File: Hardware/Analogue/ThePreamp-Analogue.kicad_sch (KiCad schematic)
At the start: 19 parts, among them J1 B1 Relays, J10 I2C (FUTURE USE), J14 12V, J15 8V, J2 PWR AMP L 12V TRIGGER, J3 PWR AMP L SWITCH, J4 PWR AMP R 12V TRIGGER, J5 PWR AMP R SWITCH, J6 PWR AMP TEMP NTC L, J7 PWR AMP TEMP NTC R, J8 MUSES 72320 (SPI), U1 AGQ20T03, U2 AGQ20T03, U3 ULN2803ADWR, U4 MCP23008-E_SO

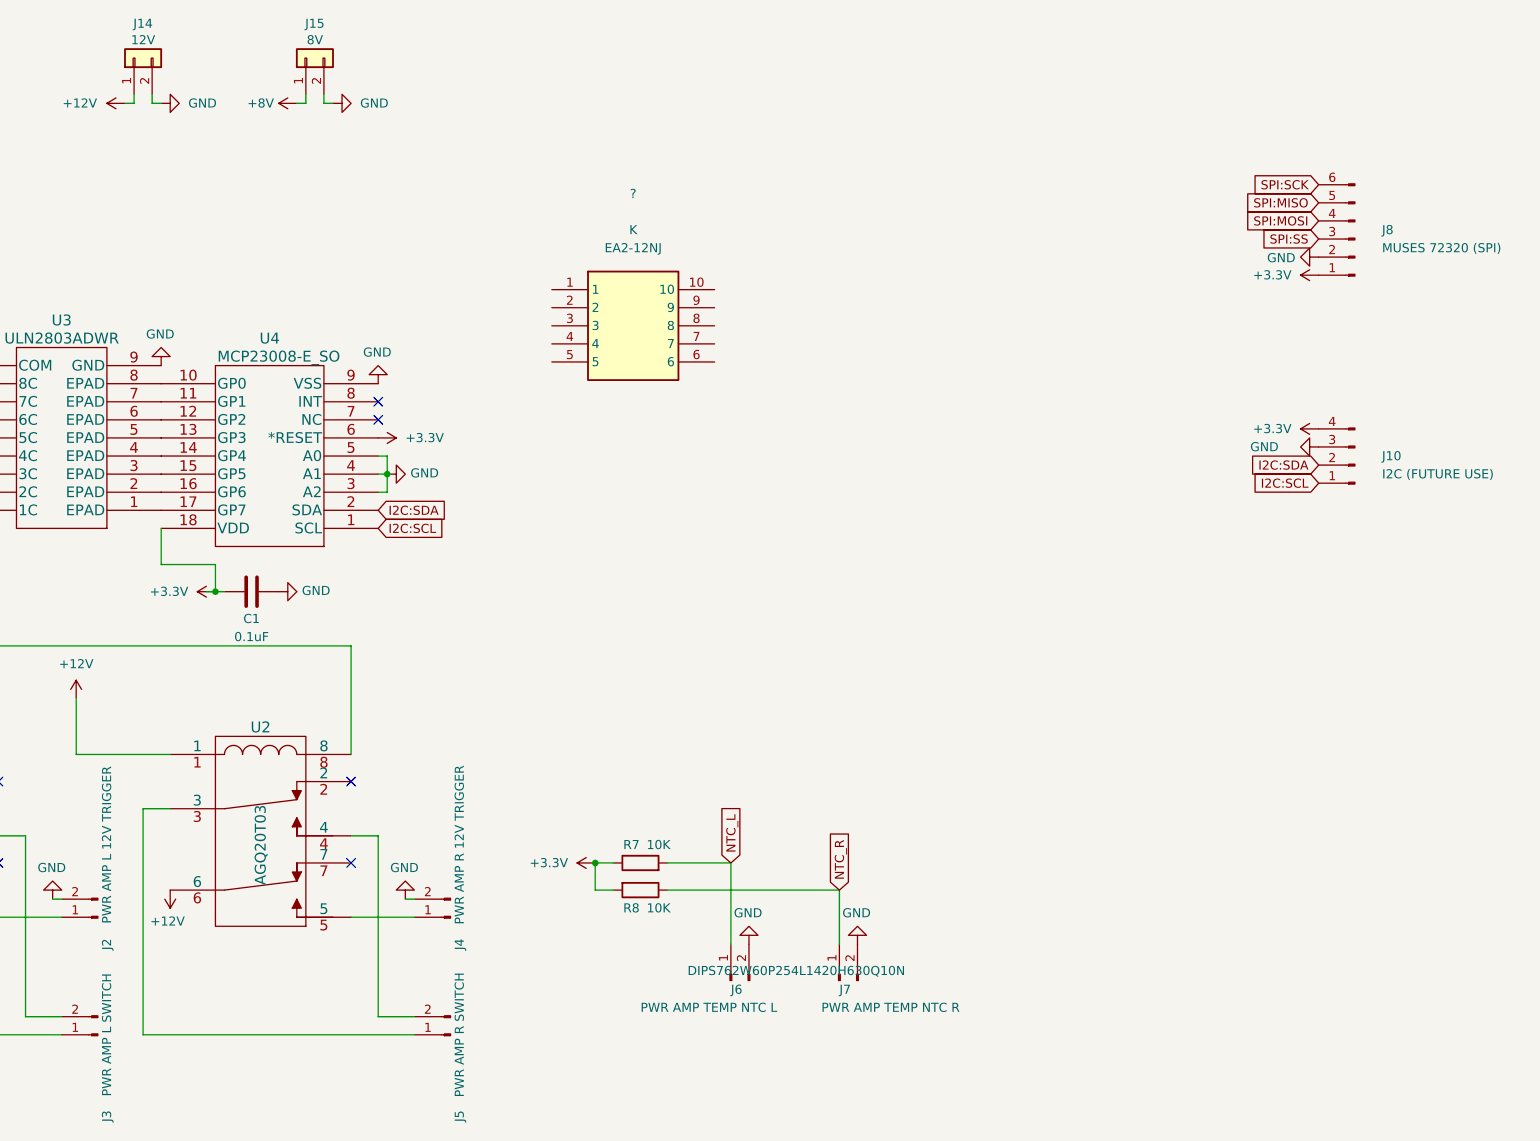
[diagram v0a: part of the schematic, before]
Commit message: added footprint to rca connector
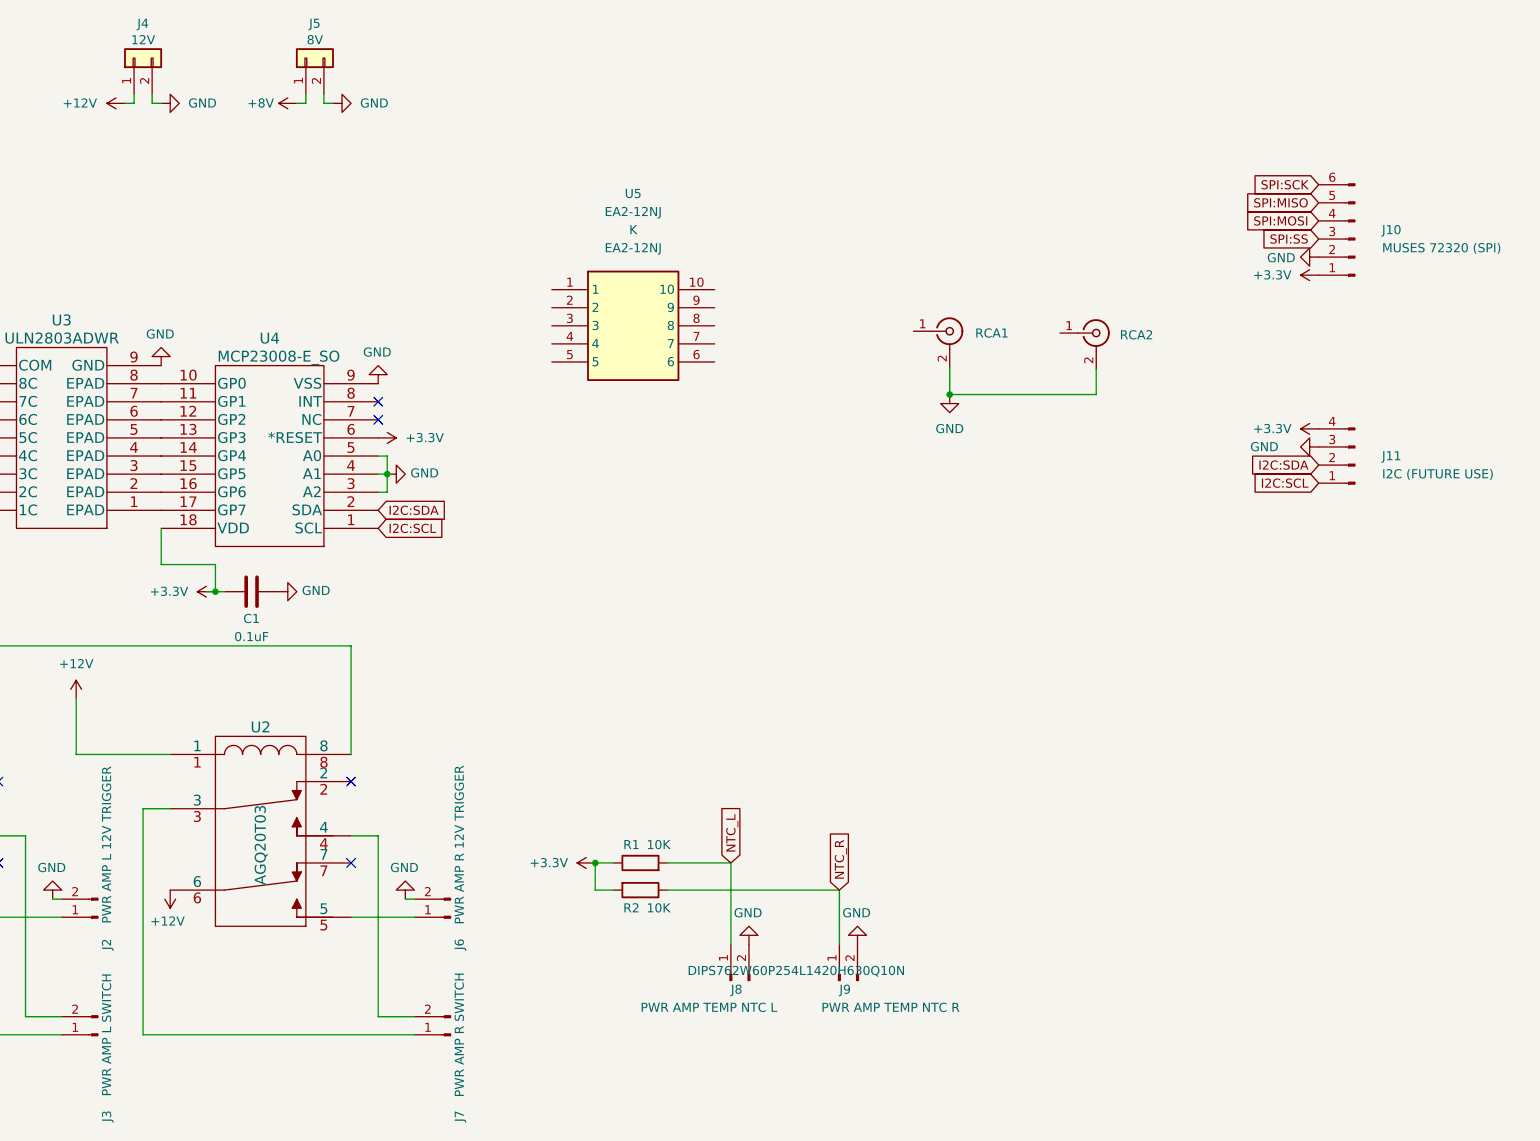
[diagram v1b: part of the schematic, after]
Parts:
- added RCA1, RCA2: (no value), symbol Connector:RCA_Connector_ALI
- U5: renamed from ?; value (none) -> EA2-12NJ
- renumbered J8 to J10, J10 to J11, J14 to J4, J15 to J5, J4 to J6, J5 to J7, J6 to J8, J7 to J9, R7 to R1, R8 to R2
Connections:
- net GND: now also RCA1.2 (Ext), RCA2.2 (Ext)

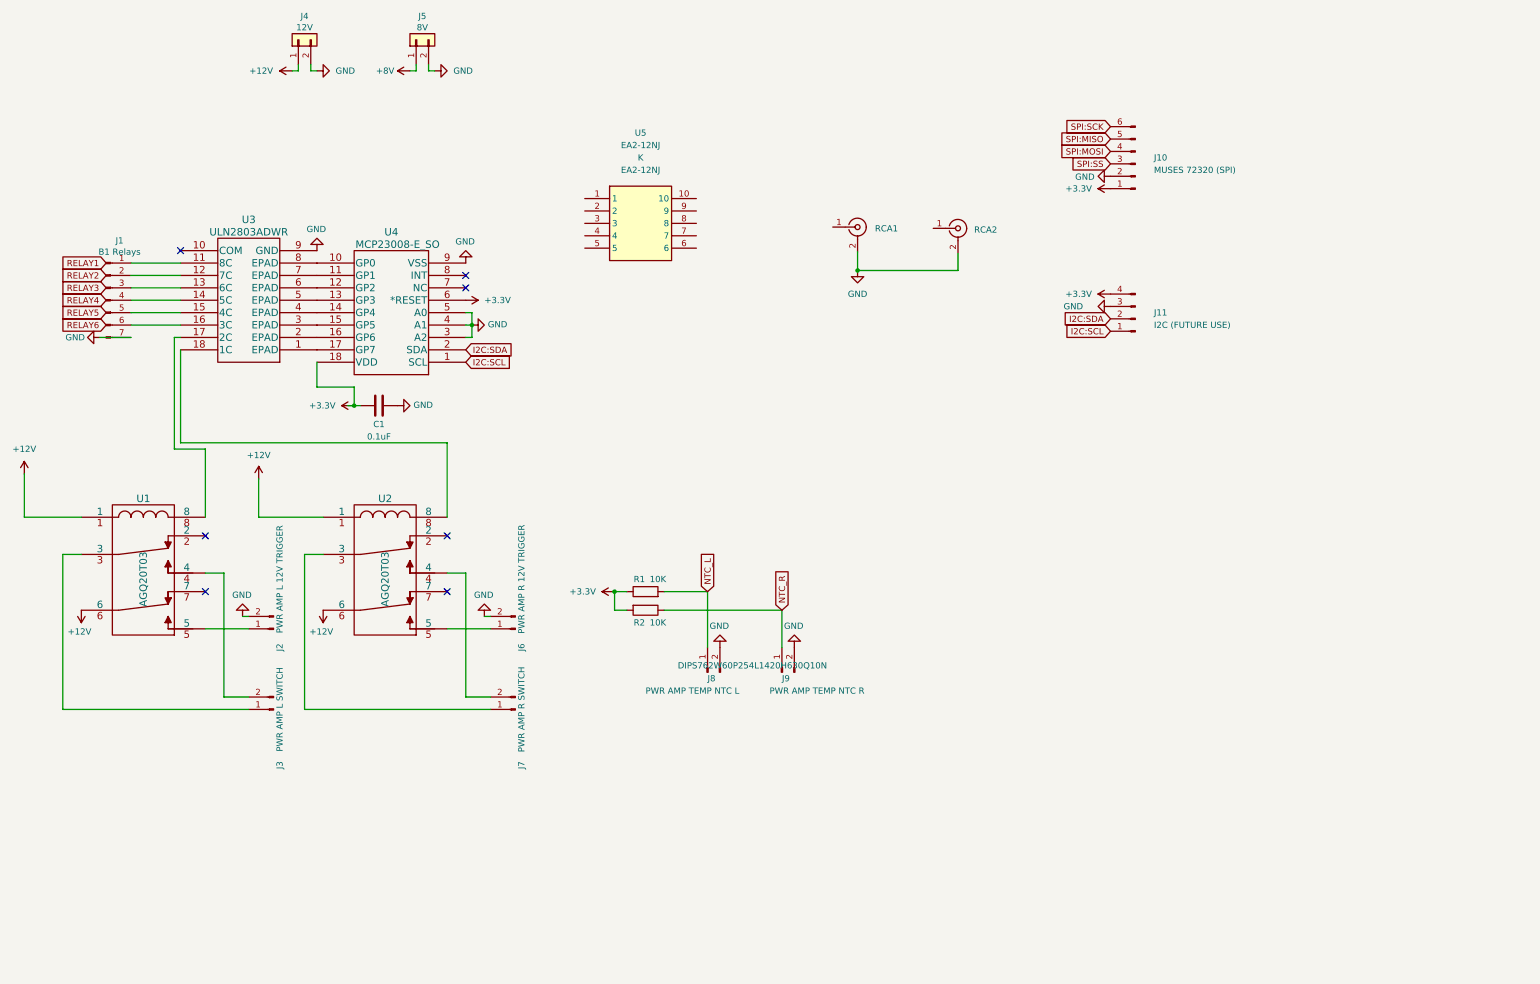
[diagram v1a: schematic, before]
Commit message: Added input section
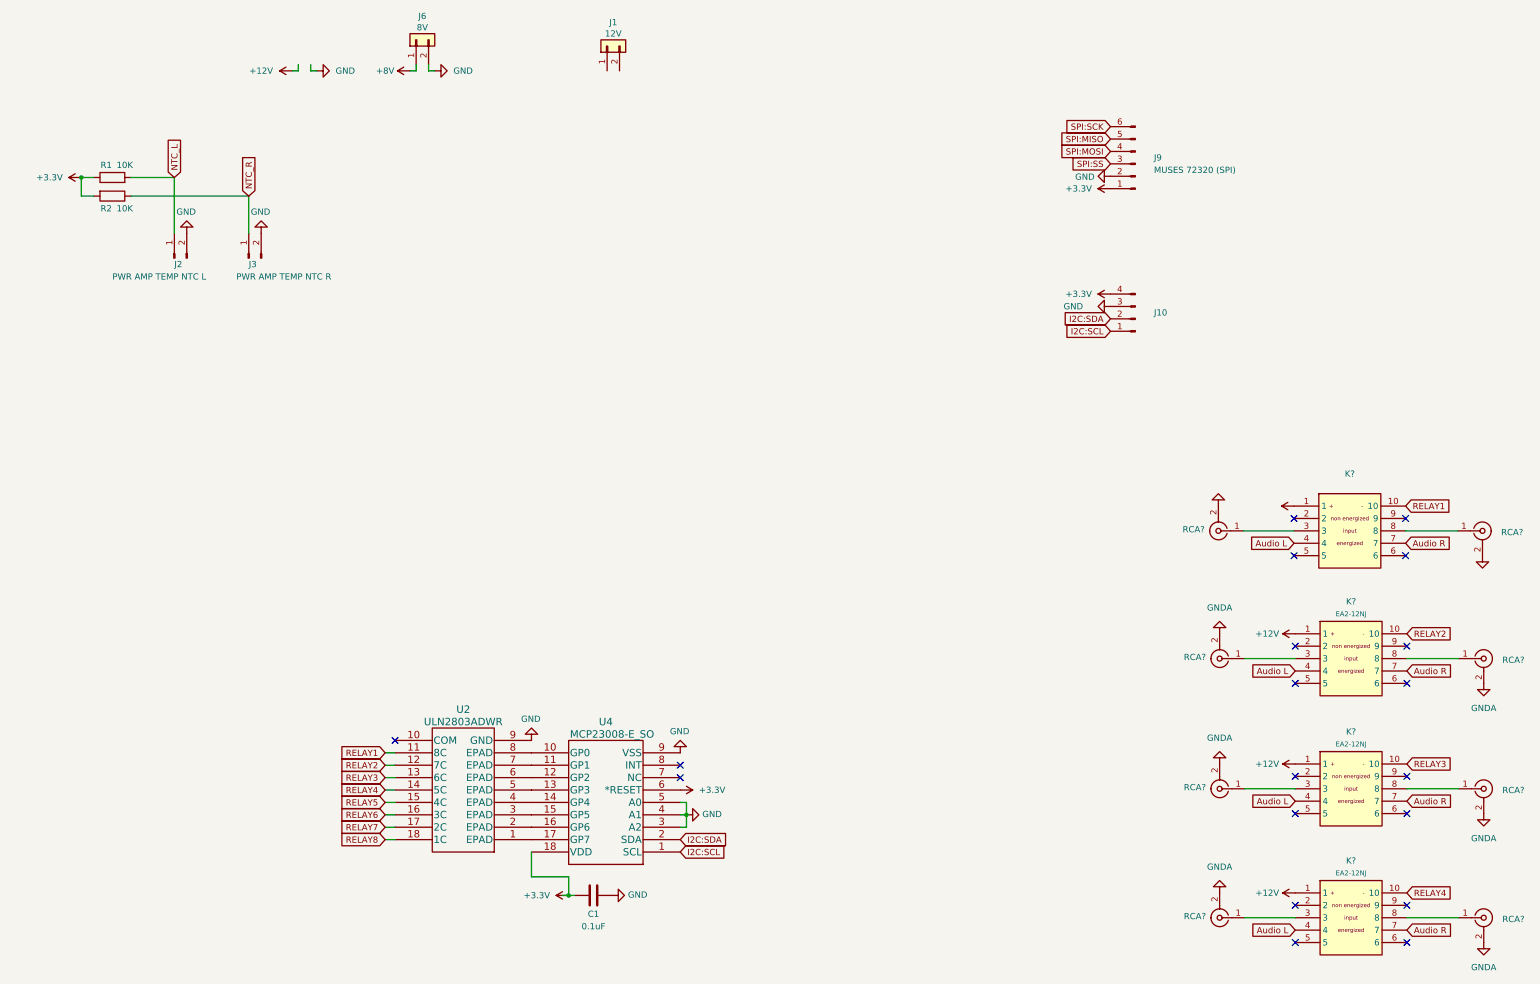
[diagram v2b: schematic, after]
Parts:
- removed J1: B1 Relays, Connector_JST:JST_XH_B7B-XH-A_1x07_P2.50mm_Vertical, symbol Connector:Conn_01x07_Male
- removed J2: PWR AMP L 12V TRIGGER, Connector_JST:JST_XH_B2B-XH-A_1x02_P2.50mm_Vertical, symbol Connector:Conn_01x02_Male
- removed J3: PWR AMP L SWITCH, Connector_JST:JST_XH_B2B-XH-A_1x02_P2.50mm_Vertical, symbol Connector:Conn_01x02_Male
- removed J6: PWR AMP R 12V TRIGGER, Connector_JST:JST_XH_B2B-XH-A_1x02_P2.50mm_Vertical, symbol Connector:Conn_01x02_Male
- removed J7: PWR AMP R SWITCH, Connector_JST:JST_XH_B2B-XH-A_1x02_P2.50mm_Vertical, symbol Connector:Conn_01x02_Male
- removed RCA1, RCA2: (no value), symbol Connector:RCA_Connector_ALI
- removed U1, U2: AGQ20T03, AGQ20T03_footprint:AGQ20012, symbol Mezmerize_B1_Controller-rescue:AGQ20012-2019-11-30_08-42-06
- removed U5: EA2-12NJ, symbol EA2-12NJ:EA2-12NJ
- added K? (x3): EA2-12NJ, symbol EA2-12NJ:EA2-12NJ
- added K?: (no value), symbol EA2-12NJ:EA2-12NJ
- added RCA? (x2): (no value), symbol Connector:RCA_Connector_ALI
- added RCA? (x6): RCA_Connector_ALI, Connector_Audio:RCA Connector ALI, symbol Connector:RCA_Connector_ALI
- J10: renamed from J11; value I2C (FUTURE USE) -> (none)
- renumbered J4 to J1, J8 to J2, J9 to J3, J5 to J6, J10 to J9, U3 to U2
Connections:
- net +12V: now also K?.1, K?.1, K?.1, K?.1; no longer J1.1 (Pin_1)
- net GND: no longer J1.2 (Pin_2)
- net RELAY1: now also U2.11 (8C), K?.10
- net RELAY2: now also U2.12 (7C), K?.10
- net RELAY3: now also U2.13 (6C), K?.10
- net RELAY4: now also U2.14 (5C), K?.10
- net RELAY5: now also U2.15 (4C)
- net RELAY6: now also U2.16 (3C)
- net RELAY7: now reaches U2.17 (2C)
- net RELAY8: now reaches U2.18 (1C)
- new net: K?.8, RCA?.1 (In) (x4)
- new net: K?.3, RCA?.1 (In) (x4)
- new net Audio L: K?.4, K?.4, K?.4, K?.4
- new net Audio R: K?.7, K?.7, K?.7, K?.7
- new net GNDA: RCA?.2 (Ext), RCA?.2 (Ext), RCA?.2 (Ext), RCA?.2 (Ext), RCA?.2 (Ext), RCA?.2 (Ext), RCA?.2 (Ext), RCA?.2 (Ext)
- no-connect marks 7 -> 19
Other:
- moved on the sheet: C1, J1, J2, J3, R1, R2, U2, U4

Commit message: added muses72323
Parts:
- added C?: (no value), Capacitor_THT:CP_Radial_D8.0mm_P3.50mm, symbol Device:C_Polarized
- added C?: (no value), symbol Device:C_Small
- added C? (x3): 100 uf/25V, Capacitor_THT:CP_Radial_D8.0mm_P3.50mm, symbol Device:C_Polarized
- added C?: (no value), symbol Device:C_Polarized
- added R?: (no value), symbol Device:R
- added U?: (no value), symbol muses72323:Muses_72323
- J10: value (none) -> I2C
- K?: value (none) -> EA2-12NJ
- RCA? (x2): value (none) -> RCA_Connector_ALI; footprint (none) -> Connector_Audio:RCA Connector ALI
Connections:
- net +3V3: now also C?.1, R?.2
- net Audio L: now also U?.27 (INL)
- net Audio R: now also U?.22 (INR)
- net GND: now also C?.1, C?.2, C?.2, C?.2, C?.2, C?.2, U?.1 (NC), U?.10 (R_REF), U?.12 (R_REF), U?.30 (ADR0), U?.31 (ADR1), U?.32 (D_REF), U?.5 (L_REF), U?.7 (L_REF), U?.8 (L_REF), U?.9 (R_REF)
- new net: C?.1, U?.29 (D_CAP)
- new net: C?.1, U?.15 (R_CAP)
- new net: R?.1, U?.16 (D_IN)
- new net: C?.1, U?.2 (L_CAP)
- new net +15V: C?.1, U?.21 (D_V+), U?.23 (AR_V+), U?.24 (AL_V+)
- new net -15V: C?.2, U?.25 (AR_V-), U?.26 (AL_V-), U?.28 (D_V-)

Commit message: ADD ANALOG PART
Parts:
- added C? (x4): 100 uf/25V, Capacitor_THT:CP_Radial_D8.0mm_P3.50mm, symbol Device:C_Polarized
- added C?: 10 pF, symbol Device:C
- added C? (x2): (no value), symbol Device:C
- added C?: 10 uF, symbol Device:C
- added R? (x3): (no value), symbol Device:R
- added R?: 47, symbol Device:R
- added R?: 100K, symbol Device:R
- added RCA? (x2): RCA_Connector_ALI, Connector_Audio:RCA Connector ALI, symbol Connector:RCA_Connector_ALI
- added RV?: 100k, symbol Device:R_Potentiometer
- added RV?: (no value), symbol Device:R_Potentiometer
- added U?: NE5534, symbol Amplifier_Operational:NE5534
- added U?: (no value), symbol Amplifier_Operational:NE5534
- C?: value (none) -> 10 uf/50V
- C?: value (none) -> 0,1uF
- C?: value (none) -> 100 uf/25V; footprint (none) -> Capacitor_THT:CP_Radial_D8.0mm_P3.50mm
- J9: value MUSES 72320 (SPI) -> (none)
- R?: value (none) -> 10
- U?: value (none) -> Muses_72323
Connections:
- net +15V: now also C?.1, C?.1, RV?.2, RV?.2, U?.7 (V+), U?.7 (V+)
- net -15V: now also C?.2, C?.2, U?.4 (V-), U?.4 (V-)
- net GND: now also C?.1, C?.1, C?.2, C?.2, R?.1, R?.1, R?.1, RCA?.2 (Ext), RCA?.2 (Ext)
- net SPI:MOSI: now also U?.18 (DATA)
- net SPI:SCK: now also U?.19 (CLOCK)
- net SPI:SS: now also U?.20 (LATCH)
- net R+: now reaches U?.11 (R+)
- net R+: now also C?.1
- net R-: now reaches U?.13 (R-)
- net R-: now also C?.2, U?.2 (-)
- net OUTR: now reaches U?.14 (OUTR)
- net OUTR: now also C?.1, R?.1, U?.6
- net at U?.17 (CLK_IN): now also R?.2
- net OUTL: now reaches U?.3 (OUTL)
- net OUTL: now also C?.1, R?.1, U?.6
- net L-: now reaches U?.4 (L-)
- net L-: now also C?.2, U?.2 (-)
- net L+: now reaches U?.6 (L+)
- net L+: now also C?.1
- new net: R?.2, RCA?.1 (In) (x2)
- new net: RV?.3, U?.1 (BAL) (x2)
- new net: C?.2, R?.2, U?.3 (+) (x2)
- new net: RV?.1, U?.8 (C/B) (x2)
- no-connect marks 19 -> 21
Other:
- note added: "https://ez.analog.com/interface-isolation/f/q-a/568260/spi-bus-with-adum1401"
- moved on the sheet: C1, C?, J1, J10, J2, J3, J6, J9, K?, R1, R2, R?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

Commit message: seperate kicad project for buffer
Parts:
- removed C? (x4): 100 uf/25V, Capacitor_THT:CP_Radial_D8.0mm_P3.50mm, symbol Device:C_Polarized
- removed C?: 10 pF, symbol Device:C
- removed C? (x2): (no value), symbol Device:C
- removed C?: 10 uF, symbol Device:C
- removed R? (x2): (no value), symbol Device:R
- removed R?: 47, symbol Device:R
- removed R?: 100K, symbol Device:R
- removed RV?: 100k, symbol Device:R_Potentiometer
- removed RV?: (no value), symbol Device:R_Potentiometer
- removed U?: NE5534, symbol Amplifier_Operational:NE5534
- removed U?: (no value), symbol Amplifier_Operational:NE5534
- added J7, J8, J9: Conn_01x03_Female, Connector_PinHeader_2.54mm:PinHeader_1x03_P2.54mm_Vertical, symbol Connector:Conn_01x03_Female
- added J? (x6): Conn_01x02_Female, Connector_PinHeader_2.54mm:PinHeader_1x02_P2.54mm_Vertical, symbol Connector:Conn_01x02_Female
- added J?: (no value), symbol Connector:Conn_01x10_Female
- added K?: EA2-12NJ, symbol EA2-12NJ:EA2-12NJ
- added RCA? (x2): RCA_Connector_ALI, Connector_Audio:RCA Connector ALI, symbol Connector:RCA_Connector_ALI
- J1: renamed from J2; value PWR AMP TEMP NTC L -> (none)
- J2: renamed from J3; value PWR AMP TEMP NTC R -> (none)
- J6: renamed from J9; value (none) -> SPI
- R3: renamed from R?; value (none) -> 0
- gave numbers to parts that had none: 22
- renumbered J6 to J3, J1 to J4, J10 to J5, U2 to U1, U4 to U2
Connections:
- net +12V: now also K?.1
- net +15V: now also J7.1 (Pin_1)
- net +3V3: now also J?.1 (Pin_1)
- net -15V: now also J7.3 (Pin_3)
- net Audio L: now also J?.1 (Pin_1), K?.4; no longer U3.27 (INL)
- net Audio R: now also J?.1 (Pin_1), K?.7; no longer U3.22 (INR)
- net GND: now also J7.2 (Pin_2), J?.2 (Pin_2), J?.2 (Pin_2), J?.5 (Pin_5)
- net GNDA: now also RCA?.2 (Ext), RCA?.2 (Ext)
- net I2C:SCL: now also J?.3 (Pin_3)
- net I2C:SDA: now also J?.4 (Pin_4)
- net L+: now also J8.3 (Pin_3)
- net L-: now also J8.2 (Pin_2)
- net OUTL: now also J8.1 (Pin_1)
- net OUTR: now also J9.1 (Pin_1)
- net R+: now also J9.3 (Pin_3)
- net R-: now also J9.2 (Pin_2)
- net RELAY1: now also K?.10
- net at RCA9.1 (In): now also J?.1 (Pin_1)
- net at RCA10.1 (In): now also J?.1 (Pin_1)
- net NTC_L renamed A0
- net A0: now also J?.7 (Pin_7)
- net NTC_R renamed A1
- net A1: now also J?.8 (Pin_8)
- new net: K?.8, RCA?.1 (In)
- new net: K?.3, RCA?.1 (In)
- new net A2: J?.9 (Pin_9)
- new net A3: J?.10 (Pin_10)
- new net Audio L buffer: J?.1 (Pin_1), U3.27 (INL)
- new net Audio R buffer: J?.1 (Pin_1), U3.22 (INR)
- no-connect marks 21 -> 23
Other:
- moved on the sheet: C1, J1, J2, J3, J4, R1, R2, RCA10, RCA9, U1, U2

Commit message: analogue pcb work
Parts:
- removed J? (x2): Conn_01x02_Female, Connector_PinHeader_2.54mm:PinHeader_1x02_P2.54mm_Vertical, symbol Connector:Conn_01x02_Female
- removed RCA10, RCA9: RCA_Connector_ALI, Connector_Audio:RCA Connector ALI, symbol Connector:RCA_Connector_ALI
- J1, J2: value (none) -> Replace
- J?: value (none) -> ADS1115
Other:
- moved on the sheet: K?, RCA?
